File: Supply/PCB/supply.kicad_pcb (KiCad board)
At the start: 2 copper layers, 89.5 x 36.2 mm, 30 parts, among them J1 Screw_Terminal_01x02, J2 Screw_Terminal_01x02, Q1 FDS4685, U1 LTC3864

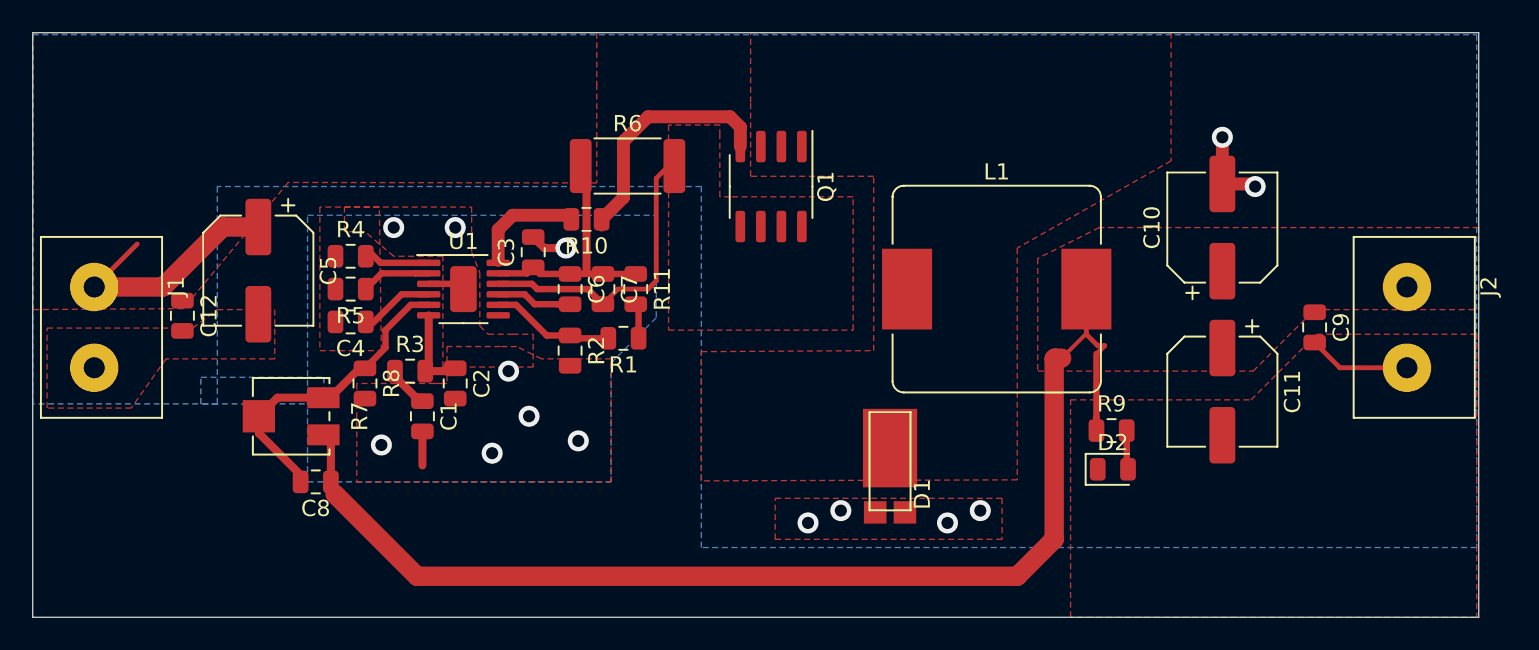
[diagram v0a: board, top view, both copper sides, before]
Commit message: PCB supply arreglos menores
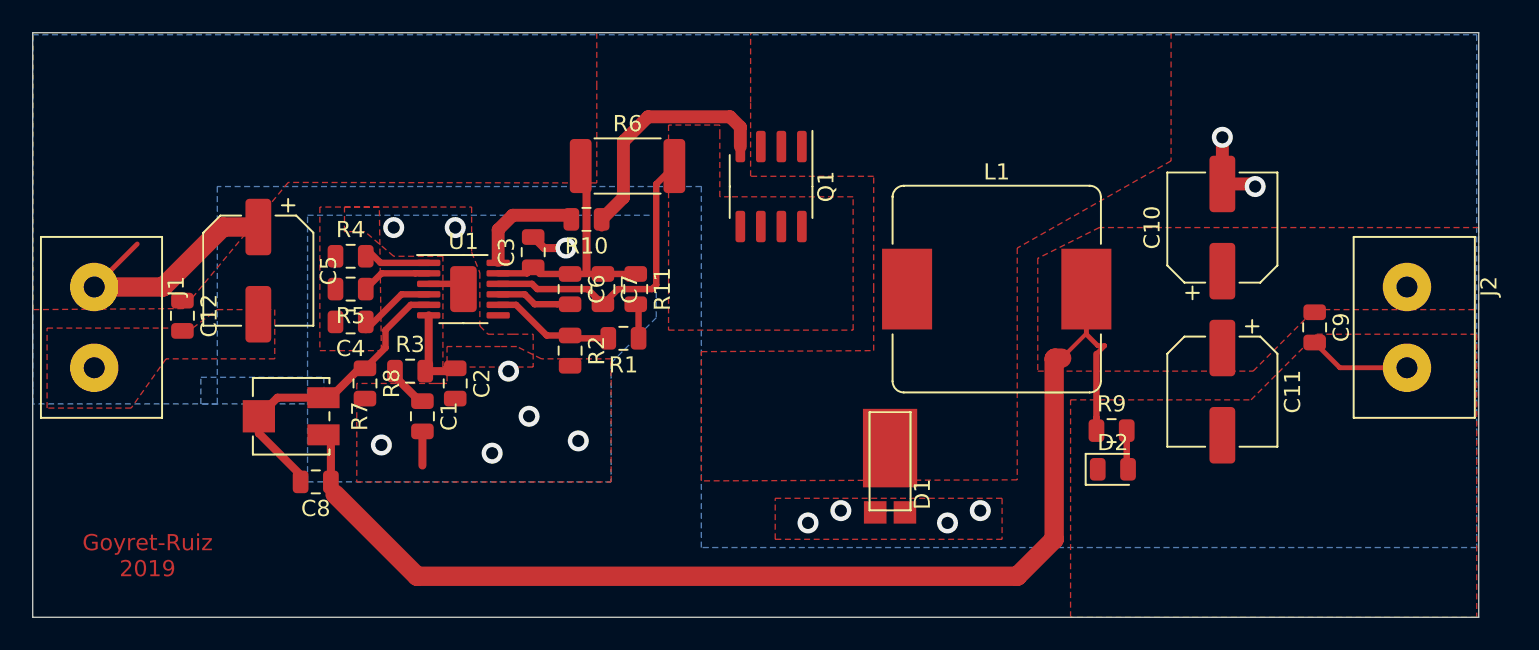
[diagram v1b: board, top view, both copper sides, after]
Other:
- board text added: "Goyret-Ruiz 2019"
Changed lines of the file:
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@@
   (general
     (thickness 1.6)
-    (drawings 4)
+    (drawings 5)
     (tracks 118)
     (zones 0)
@@
   (layers
     (0 F.Cu signal)
-    (31 B.Cu signal hide)
-    (32 B.Adhes user)
-    (33 F.Adhes user)
-    (34 B.Paste user)
-    (35 F.Paste user)
-    (36 B.SilkS user)
-    (37 F.SilkS user)
+    (31 B.Cu signal)
+    (32 B.Adhes user hide)
+    (33 F.Adhes user hide)
+    (34 B.Paste user hide)
+    (35 F.Paste user hide)
+    (36 B.SilkS user hide)
+    (37 F.SilkS user hide)
     (38 B.Mask user)
-    (39 F.Mask user)
-    (40 Dwgs.User user)
-    (41 Cmts.User user)
-    (42 Eco1.User user)
-    (43 Eco2.User user)
+    (39 F.Mask user hide)
+    (40 Dwgs.User user hide)
+    (41 Cmts.User user hide)
+    (42 Eco1.User user hide)
+    (43 Eco2.User user hide)
     (44 Edge.Cuts user)
-    (45 Margin user)
-    (46 B.CrtYd user)
-    (47 F.CrtYd user)
-    (48 B.Fab user)
+    (45 Margin user hide)
+    (46 B.CrtYd user hide)
+    (47 F.CrtYd user hide)
+    (48 B.Fab user hide)
     (49 F.Fab user hide)
   )
   (setup
-    (last_trace_width 1.2)
+    (last_trace_width 0.4)
     (user_trace_width 0.3)
     (user_trace_width 0.4)
@@
     (visible_elements 7FFFFFFF)
     (pcbplotparams
-      (layerselection 0x010fc_ffffffff)
+      (layerselection 0x00000_7fffffff)
       (usegerberextensions false)
       (usegerberattributes false)
@@
       (hpglpenspeed 20)
       (hpglpendiameter 15.000000)
-      (psnegative false)
+      (psnegative true)
       (psa4output false)
       (plotreference true)
@@
       (padsonsilk false)
       (subtractmaskfromsilk false)
-      (outputformat 1)
+      (outputformat 4)
       (mirror false)
-      (drillshape 1)
+      (drillshape 2)
       (scaleselection 1)
-      (outputdirectory ""))
+      (outputdirectory "C:/Users/Admin/Desktop/"))
   )
   (net 0 "")
@@
     (add_net "Net-(R4-Pad2)")
     (add_net "Net-(R5-Pad1)")
-    (add_net "Net-(U1-Pad7)")
     (add_net VDC)
   )
@@
       (rotate (xyz 0 0 0))
     )
+  )
+  (gr_text "Goyret-Ruiz\n2019\n" (at 112.522 104.14) (layer F.Cu)
+    (effects (font (size 1 1) (thickness 0.25)))
   )
   (gr_line (start 105.41 107.95) (end 105.41 71.755) (layer Edge.Cuts) (width 0.05))
@@
   (segment (start 135.877271 87.955) (end 136.489771 88.5675) (width 0.4) (layer F.Cu) (net 6))
   (segment (start 140.6375 88.5675) (end 140.716 88.5675) (width 0.3) (layer F.Cu) (net 7))
-  (segment (start 143.51 87.63) (end 141.6535 87.63) (width 0.3) (layer F.Cu) (net 7))
-  (segment (start 144.018 87.122) (end 143.51 87.63) (width 0.3) (layer F.Cu) (net 7))
-  (segment (start 144.018 80.772) (end 144.018 87.122) (width 0.3) (layer F.Cu) (net 7))
   (segment (start 145.14 80.01) (end 144.78 80.01) (width 0.3) (layer F.Cu) (net 7))
-  (segment (start 144.78 80.01) (end 144.018 80.772) (width 0.3) (layer F.Cu) (net 7))
   (segment (start 139.7785 87.63) (end 140.716 88.5675) (width 0.4) (layer F.Cu) (net 7))
   (segment (start 136.652 87.63) (end 139.7785 87.63) (width 0.4) (layer F.Cu) (net 7))
   (segment (start 134.23 87.305) (end 136.327 87.305) (width 0.4) (layer F.Cu) (net 7))
   (segment (start 136.327 87.305) (end 136.652 87.63) (width 0.4) (layer F.Cu) (net 7))
-  (segment (start 141.6535 87.63) (end 140.716 88.5675) (width 0.3) (layer F.Cu) (net 7))
+  (segment (start 144.018 81.132) (end 145.14 80.01) (width 0.4) (layer F.Cu) (net 7))
+  (segment (start 144.018 87.376) (end 144.018 81.132) (width 0.4) (layer F.Cu) (net 7))
+  (segment (start 143.764 87.63) (end 144.018 87.376) (width 0.4) (layer F.Cu) (net 7))
+  (segment (start 140.716 88.5675) (end 141.6535 87.63) (width 0.4) (layer F.Cu) (net 7))
+  (segment (start 141.6535 87.63) (end 143.764 87.63) (width 0.4) (layer F.Cu) (net 7))
   (segment (start 119.412 96.552) (end 119.412 95.504) (width 0.5) (layer F.Cu) (net 8))
   (segment (start 121.9985 99.568) (end 121.9985 99.1385) (width 0.5) (layer F.Cu) (net 8))
